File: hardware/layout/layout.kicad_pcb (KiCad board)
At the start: 4 copper layers, 50 x 20 mm, 73 parts, among them J1 208658-1001, J2 USB4105-GF-A-060, Q1 2N7002, SW1 TS-1088-AR02016, U1 PCA9306DCTR, U2 AP2112K-3.3TRG1, U3 USBLC6-2SC6, U4 W25Q16JVSSIQ, U5 RP2040, Y1 X322512MSB4SI

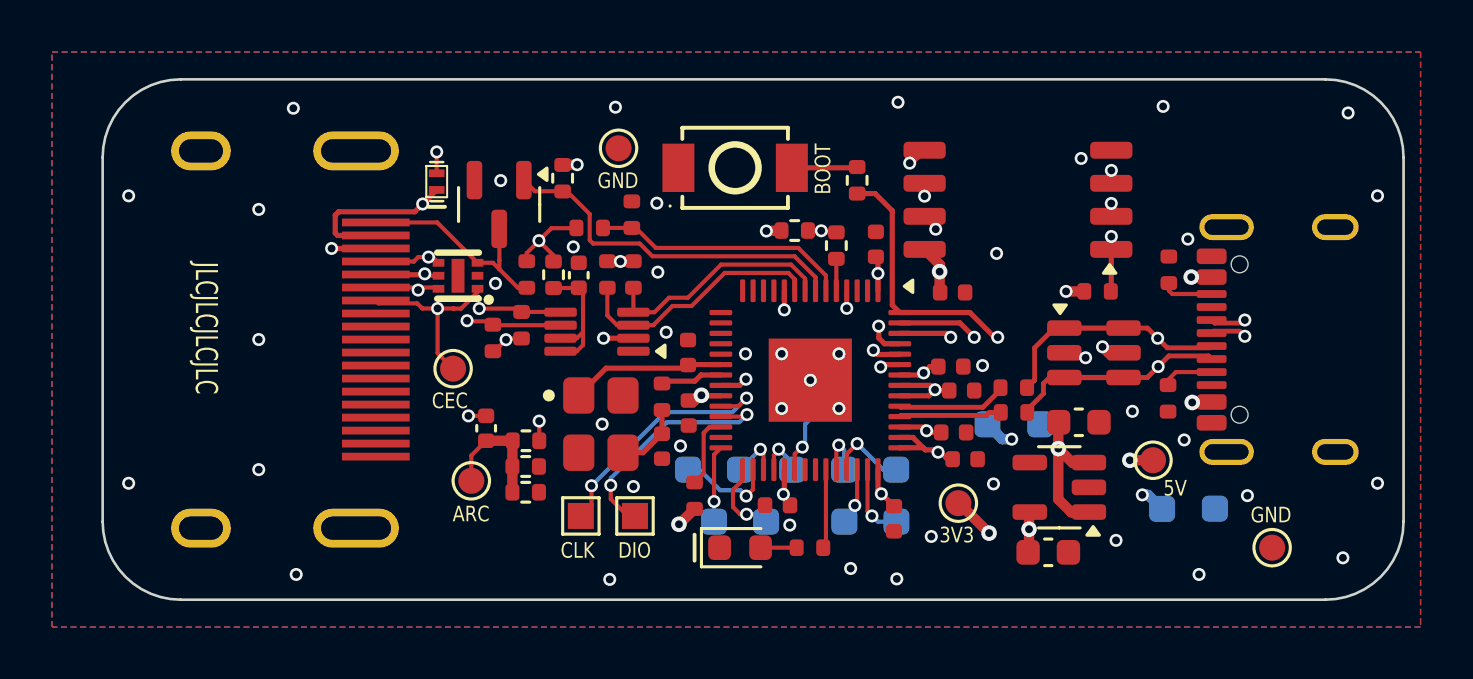
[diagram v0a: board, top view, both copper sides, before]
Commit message: hardware: swap J1/J2 to recessed mid-mount connectors on 1.2mm stack
Replace the generic top-mount connectors with sunk-board (沉板) parts
whose bodies sit in an Edge.Cuts cutout, minimising enclosure height:
  - J1 HDMI: Molex 208658-1001 -> Hong Cheng HC-HDMI0019T-3 (C7501810)
  - J2 USB-C: GCT USB4105-GF-A -> G-Switch GT-USB-7014G (C3019717)
Board thinned to 1.2mm with an explicit 4-layer stackup config, matching
the connectors' rated thickness. Adds hand-verified custom footprints
(with cutouts integrated into the board outline) and their 3D models,
and updates the jlcpcb-lcsc MPN->LCSC overlay.

Layout re-synced and brought to a clean DRC (0 violations, 0 unconnected):
  - silk reference designators hidden again after the re-sync re-enabled
    them (kept on F.Fab for PnP)
  - new midmount_connector_edge_clearance .kicad_dru rule for the parts'
    intrinsic ~0.16mm pad-to-cutout gaps
  - J1/J2 body-outline silk removed (crossed the cutouts; connectors are
    mechanically keyed)
  - stale off-board GND pour island cleared by a zone refill
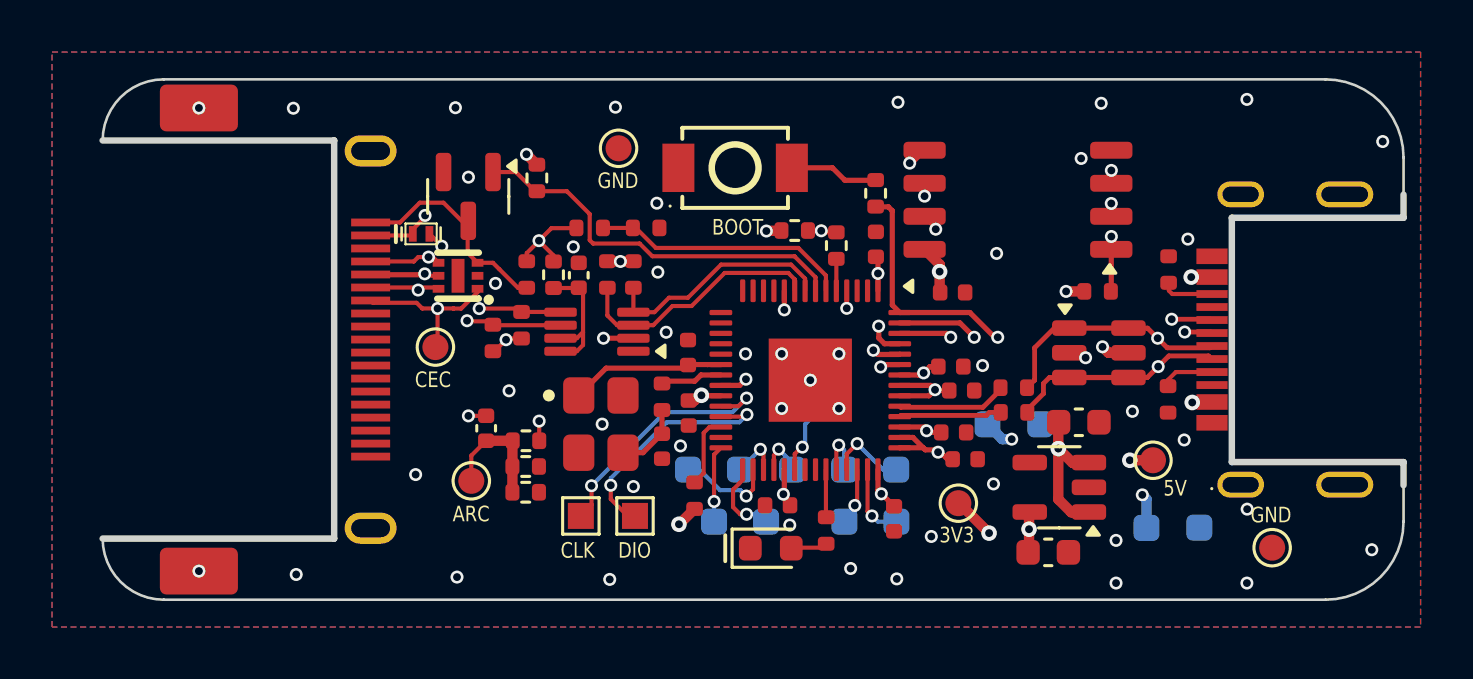
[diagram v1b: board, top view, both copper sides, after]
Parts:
- removed the TP18 at (114.2, 116.4)
- added TP17: ?, kicad_libraries_kicad-footprints_TestPoint@9.0.3:TestPoint_Pad_D1.0mm, F.Cu at (114.2, 116.4)
- J1: value 208658-1001 -> HC-HDMI0019T-3; footprint kicad_libraries_kicad-footprints_Connector_Video@9.0.3:HDMI_A_Molex_208658-1001_Horizontal -> naorunaoru_picoarc_footprints_picoarc:HDMI-SMD_HC-HDMI0019T-3_PicoARC_R6
- J2: value USB4105-GF-A-060 -> GT-USB-7014G; footprint kicad_libraries_kicad-footprints_Connector_USB@9.0.3:USB_C_Receptacle_GCT_USB4105-xx-A_16P_TopMnt_Horizontal -> naorunaoru_picoarc_footprints_picoarc:USB-C-SMD_GT-USB-7014D
- U1: value PCA9306DCTR -> PCA9306DCUR
- moved D3 2.10 mm to (112.2, 106.9), turned to 0 degrees
- moved Q1 1.23 mm to (114.1, 105.5)
- moved D1 1.18 mm to (125.7, 119.0)
- moved J2 1.12 mm to (145.2, 111.0)
- moved TP18 1.07 mm to (112.8, 111.3)
- moved R13 0.99 mm to (116.7, 104.8)
- moved TP4 0.94 mm to (142.2, 118.2)
- moved TP2 0.94 mm to (140.1, 118.2)
- moved R4 0.91 mm to (127.8, 118.3), turned to -90 degrees
- moved R16 0.87 mm to (129.7, 105.4)
- moved R7 0.75 mm to (120.9, 106.7), turned to 0 degrees
- moved U3 0.19 mm to (138.3, 111.5)
- renumbered TP16 to TP15, TP17 to TP16, TP19 to TP18, TP20 to TP19, TP21 to TP20, TP22 to TP21, TP23 to TP22
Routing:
- net HDMI._HDMI_5V: track 11.6 -> 7.53 mm
- net USB_D_N: track 14.0 -> 11.3 mm
- net USB_D_P: track 14.1 -> 11.8 mm
- net GND: track 2.52 -> 0.67 mm
- net HPD_GATE: track 13.9 -> 15.2 mm
- net STATUS_LED: track 3.04 -> 1.83 mm
- net QSPI_CS: track 18.1 -> 17.2 mm
- net BOOTSEL_SW: track 2.52 -> 3.42 mm
- net CEC_NODE: track 25.0 -> 24.2 mm
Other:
- outline, holes or cut-outs redrawn
- board text removed: "JLCJLCJLCJLC"

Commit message: hardware: add picoprobe debug connector
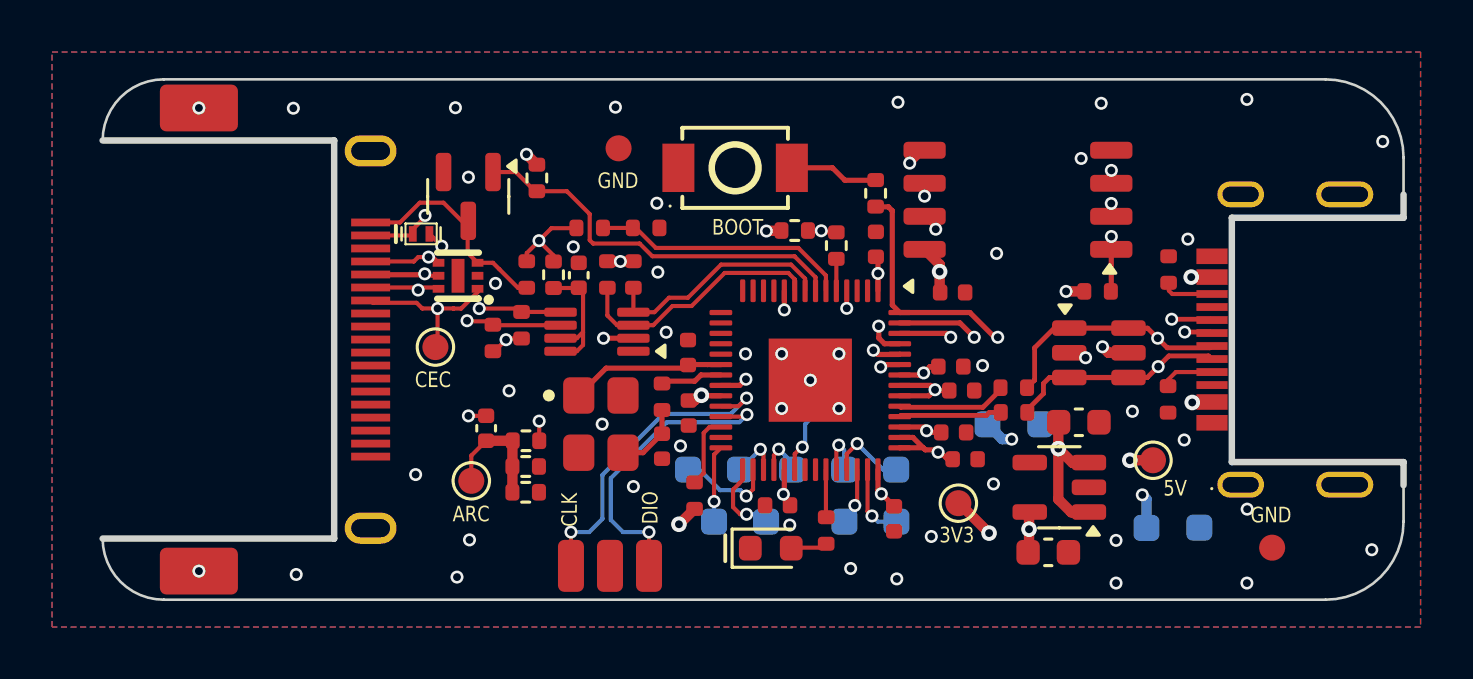
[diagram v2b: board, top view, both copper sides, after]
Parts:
- removed the TP19 at (144.9, 119.0)
- removed TP22: ?, kicad_libraries_kicad-footprints_TestPoint@9.0.3:TestPoint_Pad_1.0x1.0mm
- added TP15: ?, naorunaoru_picoarc_footprints_picoarc:SWD_EdgePads_1x03_P1.50mm, F.Cu at (119.5, 119.7)
- TP20: footprint kicad_libraries_kicad-footprints_TestPoint@9.0.3:TestPoint_Pad_D1.0mm -> naorunaoru_picoarc_footprints_picoarc:TestPad_D1.0mm_Round_Thermal
- TP21: footprint kicad_libraries_kicad-footprints_TestPoint@9.0.3:TestPoint_Pad_1.0x1.0mm -> naorunaoru_picoarc_footprints_picoarc:TestPad_D1.0mm_Round_Thermal
- TP3, TP4: footprint naorunaoru_picoarc_footprints_picoarc:TestPad_1.0x1.0mm_RoundRect -> naorunaoru_picoarc_footprints_picoarc:TestPad_1.0x1.0mm_RoundRect_Thermal
- moved TP20 29.4 mm to (144.9, 119.0)
- moved TP21 14.2 mm to (119.8, 103.7)
- renumbered TP15 to TP16, TP16 to TP17, TP17 to TP18, TP18 to TP19
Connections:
- TP21 pad 1: SWD_SWCLK -> GND
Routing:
- net SWD_SWDIO: track 9.28 -> 11.8 mm
- net SWD_SWCLK: track 9.80 -> 12.3 mm
